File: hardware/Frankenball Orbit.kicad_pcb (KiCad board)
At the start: 2 copper layers, 91.9 x 57.4 mm, 44 parts, among them J1 Conn_02x03_Odd_Even, J101 ADNS-5050, J102 Conn_01x05_Male, J103 Conn_02x04_Odd_Even, J2 Connector_Generic:Conn_01x05, Q101 PT2559B, Q102 2N7002, SW1 SW_Push, SW101 SW_Push, SW102 SW_Push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

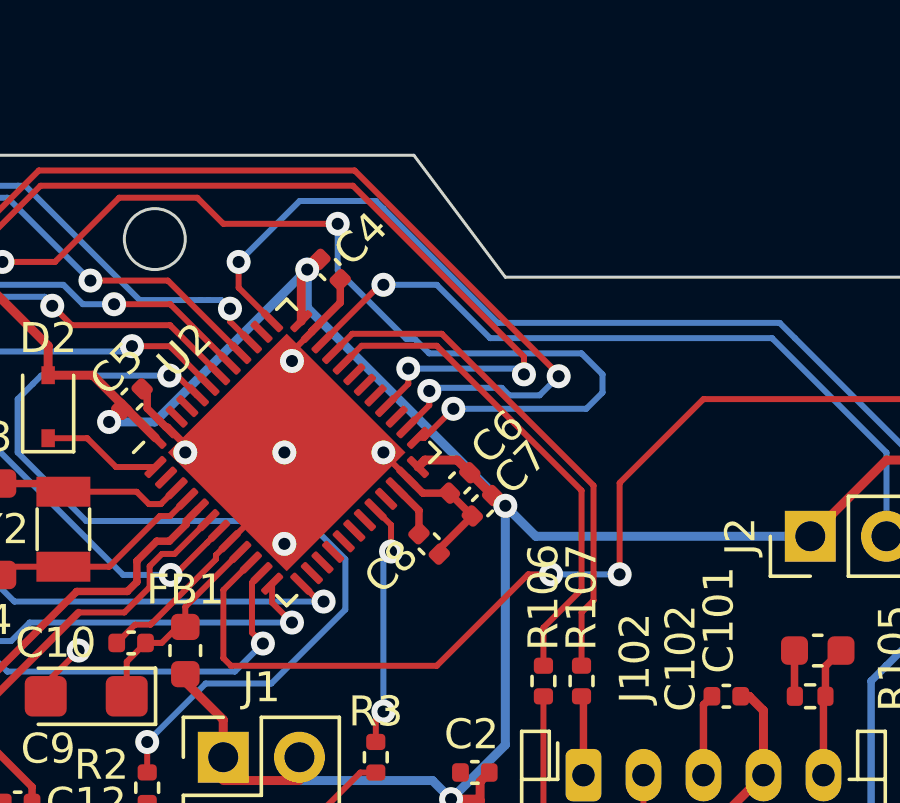
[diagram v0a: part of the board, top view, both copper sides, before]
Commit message: Added more filtering caps to STM32 supply
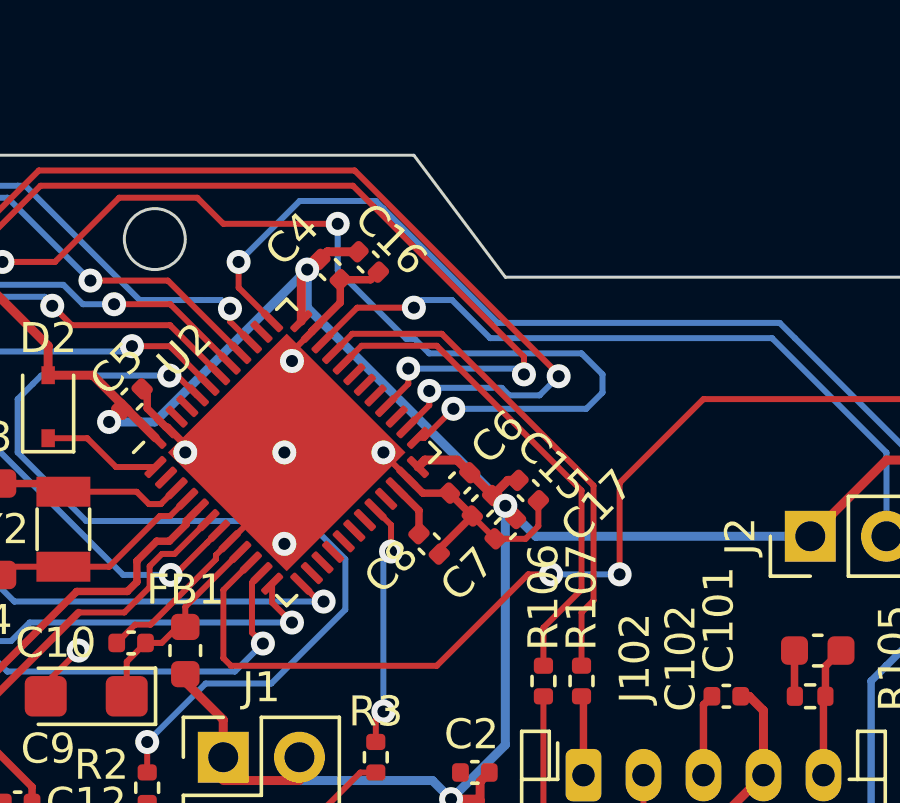
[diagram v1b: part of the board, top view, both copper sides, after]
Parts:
- added C15: 100nF, Capacitor_SMD:C_0402_1005Metric, F.Cu at (159.8, 84.8)
- added C16: 100nF, Capacitor_SMD:C_0402_1005Metric, F.Cu at (154.4, 77.2)
- added C17: 4.7uF, Capacitor_SMD:C_0402_1005Metric, F.Cu at (159.0, 86.1)
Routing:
- net GND: track 28.5 -> 33.4 mm
- net +3V3: track 150.9 -> 154.4 mm
